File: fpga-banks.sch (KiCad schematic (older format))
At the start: 59 parts, among them J13 62000311121, Q12 2N7002, Q13 2N7002, Q14 2N7002, Q15 2N7002, Q16 2N7002, U14 XC7A100T-FGG484, U15 AMJMEFB-100.0000T

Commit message: Update schematic notes, update SPI0 connection
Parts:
- removed R113: R_0R_0402, artix-dc-scm-footprints:0402-res, symbol artix-dc-scm:R_0R_0402
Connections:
- net labels removed: PRSNT1_N, PRSNT1_N_R
- wire segments 404 -> 402
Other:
- note removed: "FPGA connections to be established while preparing layout"
- note removed: "Interfaces status:\nJTAG - needs pre-defined pins (BANK0)\nboot (Q)SPI - needs pre-defined pins (BANK14)\neSPI\nQSPI0, QSPI1 - \nSPI - \nSGPIO0, SGPIO1 - \nUSB client, USB host - free\nPCIe x1 - needs to be connected to transreceivers\nI3C - free\nI2C - free\nNCSI-\nUART \nethernet - free\nDDR3 - uses B34 as in references\neMMC - free"
- note removed: "done"
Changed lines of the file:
@@
 Text GLabel 9700 4350 2    50   Input ~ 0
 UART0_SCM_RX
-Text Notes 2425 650  0    50   ~ 0
-FPGA connections to be established while preparing layout
 Wire Wire Line
 	1425 8600 1800 8600
@@
 Text GLabel 2200 10025 2    50   Input ~ 0
 IRQ_N
-Text GLabel 2200 10225 2    50   Input ~ 0
-PRSNT1_N
 Wire Wire Line
 	11600 3500 12000 3500
@@
 $EndComp
 $Comp
-L artix-dc-scm:R_0R_0402 R113
-U 1 1 6154FB1E
-P 1950 10225
-F 0 "R113" H 1950 10325 60  0000 C CNN
-F 1 "R_0R_0402" H 1950 10075 60  0001 C CNN
-F 2 "artix-dc-scm-footprints:0402-res" H 2150 10425 60  0001 L CNN
-F 3 "" H 1950 10225 50  0001 C CNN
-F 4 "PANASONIC" H 2150 10625 60  0001 L CNN "Manufacturer"
-F 5 "ERJ2GE0R00X" H 2150 10525 60  0001 L CNN "MPN"
-F 6 "0R" H 1950 10225 50  0000 C CNN "Val"
-	1    1950 10225
-	1    0    0    -1
-$EndComp
-$Comp
 L artix-dc-scm:R_0R_0402 R108
 U 1 1 6154DC81
@@
 Wire Wire Line
 	2100 10025 2200 10025
-Wire Wire Line
-	2100 10225 2200 10225
 Text GLabel 3950 7800 2    50   Input ~ 0
 PRSNT0_N
@@
 Text GLabel 9825 6450 2    50   Input ~ 0
 USR_LED2
-Text Notes 13100 8900 0    50   ~ 0
-Interfaces status:\nJTAG - needs pre-defined pins (BANK0)\nboot (Q)SPI - needs pre-defined pins (BANK14)\neSPI\nQSPI0, QSPI1 - \nSPI - \nSGPIO0, SGPIO1 - \nUSB client, USB host - free\nPCIe x1 - needs to be connected to transreceivers\nI3C - free\nI2C - free\nNCSI-\nUART \nethernet - free\nDDR3 - uses B34 as in references\neMMC - free
-Text Notes 12900 7750 0    50   ~ 10
-done
-Text Notes 12900 7850 0    50   ~ 10
-done
-Text Notes 12900 8325 0    50   ~ 10
-done
-Text Notes 12900 8825 0    50   ~ 10
-done
 Wire Wire Line
 	14800 4200 14900 4200
 Wire Wire Line
 	14800 3800 14900 3800
-Text Notes 12900 8250 0    50   ~ 10
-done
-Text Notes 12900 8900 0    50   ~ 10
-done
 Wire Wire Line
 	2200 9225 2100 9225
-Text Notes 12900 8025 0    50   ~ 10
-done
-Text Notes 12900 8425 0    50   ~ 10
-done
-Text Notes 12900 8675 0    50   ~ 10
-done
-Text Notes 12900 8175 0    50   ~ 10
-done
-Text Notes 12900 8500 0    50   ~ 10
-done
-Text Notes 12900 8575 0    50   ~ 10
-done
-Text Notes 12900 8100 0    50   ~ 10
-done
 Wire Wire Line
 	4150 1250 4625 1250
@@
 	1    0    0    -1
 $EndComp
-Text Notes 12900 7925 0    50   ~ 10
-done
 $Comp
 L artix-dc-scm:R_0R_0402 R144
@@
 	1    0    0    -1
 $EndComp
-Wire Wire Line
-	1800 10225 1425 10225
 Wire Wire Line
 	1800 10425 1425 10425
@@
 Text GLabel 1425 10025 0    50   Input ~ 0
 IRQ_N_R
-Text GLabel 1425 10225 0    50   Input ~ 0
-PRSNT1_N_R
 Text GLabel 1425 10425 0    50   Input ~ 0
 SPARE1_R

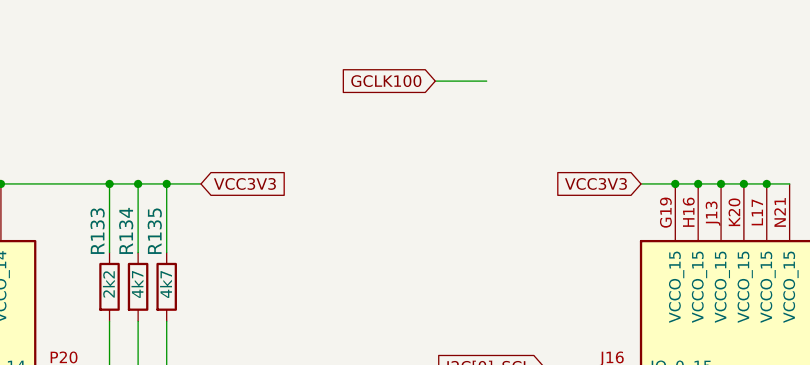
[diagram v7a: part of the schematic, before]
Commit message: Update filtering capacitors
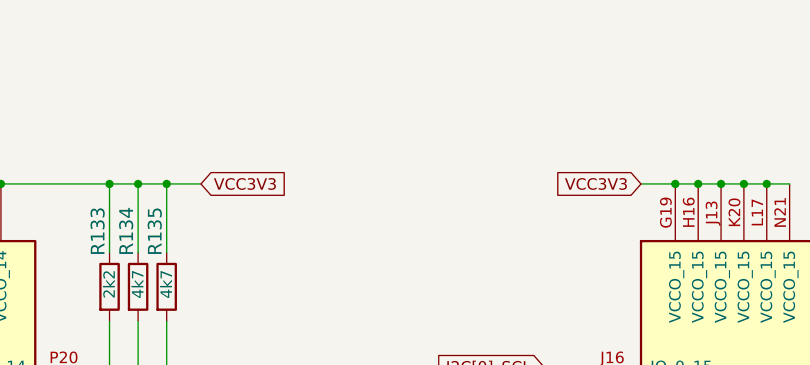
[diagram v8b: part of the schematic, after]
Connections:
- wire segments 402 -> 401
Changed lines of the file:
@@
 Wire Wire Line
 	15175 9225 15225 9225
-Wire Wire Line
-	6275 800  6050 800
-Text GLabel 6050 800  0    50   Input ~ 0
-GCLK100
 Text GLabel 9825 4550 2    50   Input ~ 0
 GCLK100
